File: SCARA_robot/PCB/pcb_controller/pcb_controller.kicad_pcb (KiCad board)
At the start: 2 copper layers, 24 parts, among them IC1 LD1117-3.3V-SOT223, J1 Barrel_Jack_Switch, J2 Conn_01x04_Pin_STEPPER_A, U1 LM7805CT, U2 ESP32-DEVKIT-V1

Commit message: schematic ready
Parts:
- added A2: Pololu_Breakout_DRV8825, Module:Pololu_Breakout-16_15.2x20.3mm, F.Cu at (224.3, 70.8)
- added A3: Pololu_Breakout_DRV8825, Module:Pololu_Breakout-16_15.2x20.3mm, F.Cu at (224.7, 46.5)
- added J10: interface, Connector_PinHeader_2.54mm:PinHeader_1x04_P2.54mm_Vertical, F.Cu at (126.6, 60.9)
- added J11: Conn_01x07_Socket, Connector_JST:JST_XH_S7B-XH-A-1_1x07_P2.50mm_Horizontal, F.Cu at (158.6, 139.5)
- added J12: Encoder_A, Connector_JST:JST_XH_B7B-XH-AM_1x07_P2.50mm_Vertical, F.Cu at (118.6, 28.9)
- added J13: Encoder_B, Connector_JST:JST_XH_B7B-XH-AM_1x07_P2.50mm_Vertical, F.Cu at (118.6, 36.7)
- added J14: Encoder_C, Connector_JST:JST_XH_B7B-XH-AM_1x07_P2.50mm_Vertical, F.Cu at (118.6, 44.5)
- added J15: Conn_01x04_Pin_STEPPER_B, Connector_JST:JST_XH_B4B-XH-AM_1x04_P2.50mm_Vertical, F.Cu at (115.3, 116.9)
- added J16: Conn_01x04_Pin_STEPPER_C, Connector_JST:JST_XH_B4B-XH-AM_1x04_P2.50mm_Vertical, F.Cu at (115.3, 124.7)
- added J3: interface, Connector_PinHeader_2.54mm:PinHeader_1x04_P2.54mm_Vertical, F.Cu at (157.8, 125.3)
- added J4: power, Connector_PinHeader_2.54mm:PinHeader_1x03_P2.54mm_Vertical, F.Cu at (117.4, 51.2)
- added J5: Conn_01x07_Socket, Connector_JST:JST_XH_S7B-XH-A-1_1x07_P2.50mm_Horizontal, F.Cu at (96.6, 30.4)
- added J6: power, Connector_PinHeader_2.54mm:PinHeader_1x03_P2.54mm_Vertical, F.Cu at (122.0, 51.2)
- added J7: interface, Connector_PinHeader_2.54mm:PinHeader_1x04_P2.54mm_Vertical, F.Cu at (122.0, 60.9)
- added J8: Conn_01x07_Socket, Connector_JST:JST_XH_S7B-XH-A-1_1x07_P2.50mm_Horizontal, F.Cu at (96.6, 44.0)
- added J9: power, Connector_PinHeader_2.54mm:PinHeader_1x03_P2.54mm_Vertical, F.Cu at (126.6, 51.2)
- added JP1: sel_encoderA, Jumper:SolderJumper-3_P1.3mm_Open_RoundedPad1.0x1.5mm, F.Cu at (131.7, 60.3)
- added JP2: sel_encoderB, Jumper:SolderJumper-3_P1.3mm_Open_RoundedPad1.0x1.5mm, F.Cu at (131.7, 64.2)
- added JP3: sel_encoderC, Jumper:SolderJumper-3_P1.3mm_Open_RoundedPad1.0x1.5mm, F.Cu at (131.7, 68.0)
- added JP4: SolderJumper_2_Open, Jumper:SolderJumper-2_P1.3mm_Open_RoundedPad1.0x1.5mm, F.Cu at (131.1, 53.8)
- added JP5: SolderJumper_2_Open, Jumper:SolderJumper-2_P1.3mm_Open_RoundedPad1.0x1.5mm, F.Cu at (124.8, 93.4)
- added JP6: SolderJumper_2_Open, Jumper:SolderJumper-2_P1.3mm_Open_RoundedPad1.0x1.5mm, F.Cu at (124.8, 97.0)
- added R10: 10K, PCM_Resistor_THT_AKL:R_Axial_DIN0204_L3.6mm_D1.6mm_P5.08mm_Horizontal, F.Cu at (130.3, 50.5)
- added SW1: Microstep mode, Button_Switch_THT:SW_DIP_SPSTx03_Slide_9.78x9.8mm_W7.62mm_P2.54mm, F.Cu at (106.2, 80.8)
- added SW2: Microstep mode, Button_Switch_THT:SW_DIP_SPSTx03_Slide_9.78x9.8mm_W7.62mm_P2.54mm, F.Cu at (90.9, 116.7)
- added SW3: Microstep mode, Button_Switch_THT:SW_DIP_SPSTx03_Slide_9.78x9.8mm_W7.62mm_P2.54mm, F.Cu at (102.3, 116.7)
- moved A1 154.6 mm to (224.2, 93.4)
- moved U2 129.3 mm to (172.7, 74.6)
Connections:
- A1 pad 13: unconnected-(A1-~{RST}-Pad13) -> /baseM_rst
- A1 pad 14: unconnected-(A1-~{SLP}-Pad14) -> Net-(A1-~{SLP})
- A1 pad 15: unconnected-(A1-STEP-Pad15) -> /baseM_step
- A1 pad 16: unconnected-(A1-DIR-Pad16) -> /baseM_dir
- A1 pad 2: unconnected-(A1-~{FLT}-Pad2) -> Net-(A1-~{FLT})
- R1 pad 2: unconnected-(R1-Pad2) -> /sda_master
- R2 pad 2: unconnected-(R2-Pad2) -> /scl_master
- R4 pad 2: unconnected-(R4-Pad2) -> /sda_enA
- R5 pad 2: unconnected-(R5-Pad2) -> /scl_enA
- R6 pad 2: unconnected-(R6-Pad2) -> /sda_enB
- R7 pad 2: unconnected-(R7-Pad2) -> /scl_enB
- R8 pad 2: unconnected-(R8-Pad2) -> /sda_enC
- R9 pad 2: unconnected-(R9-Pad2) -> /scl_enC
- U2 pad 11: unconnected-(U2-D21-Pad11) -> /sda_master
- U2 pad 14: unconnected-(U2-D22-Pad14) -> /scl_master

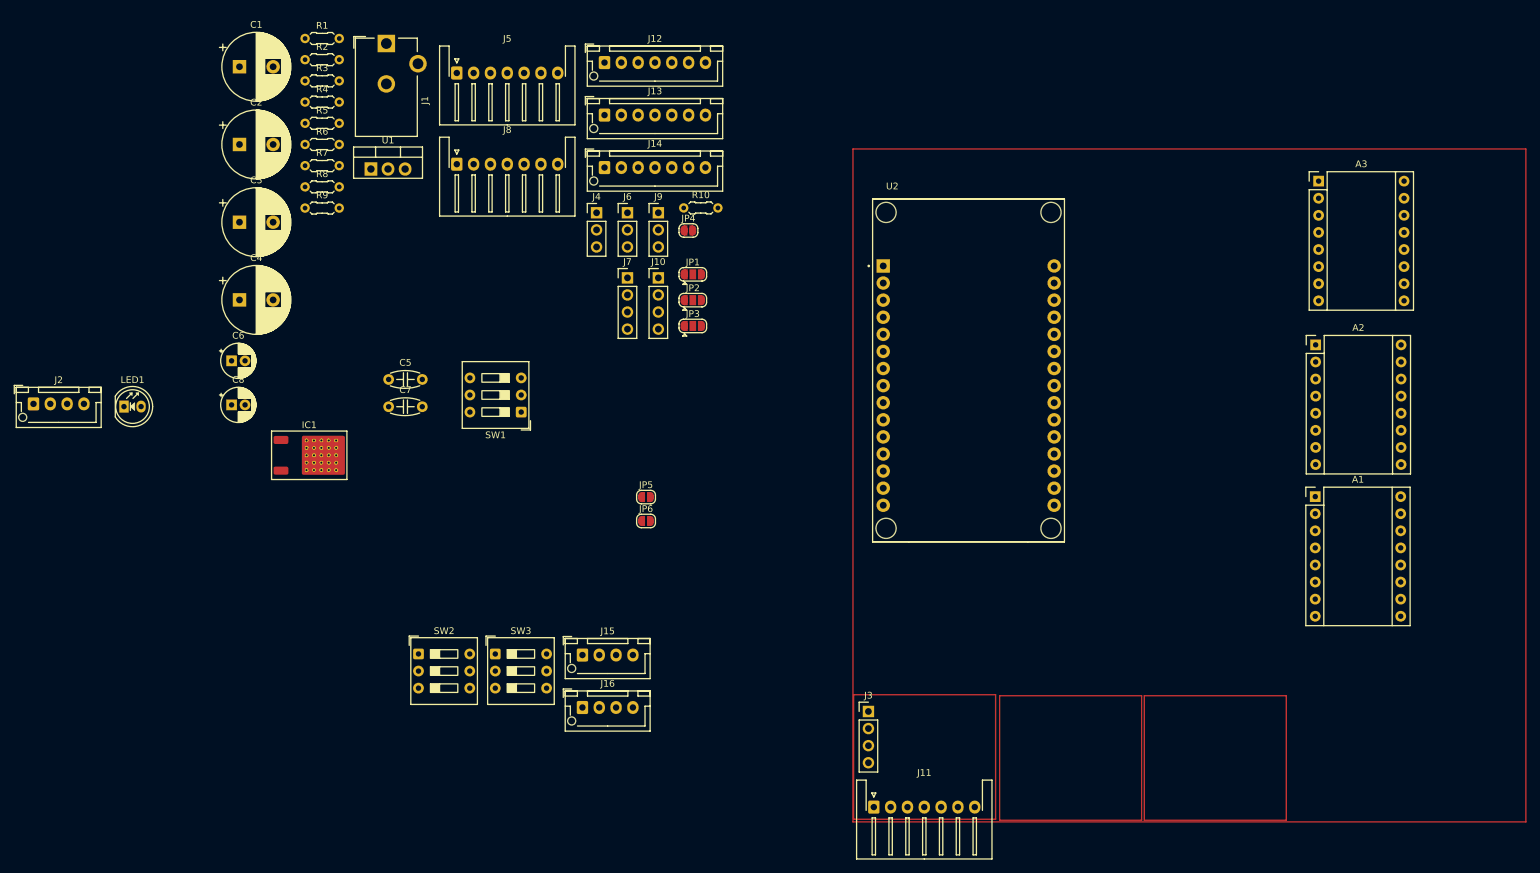
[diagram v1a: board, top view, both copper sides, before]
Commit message: schematic and footprints ready
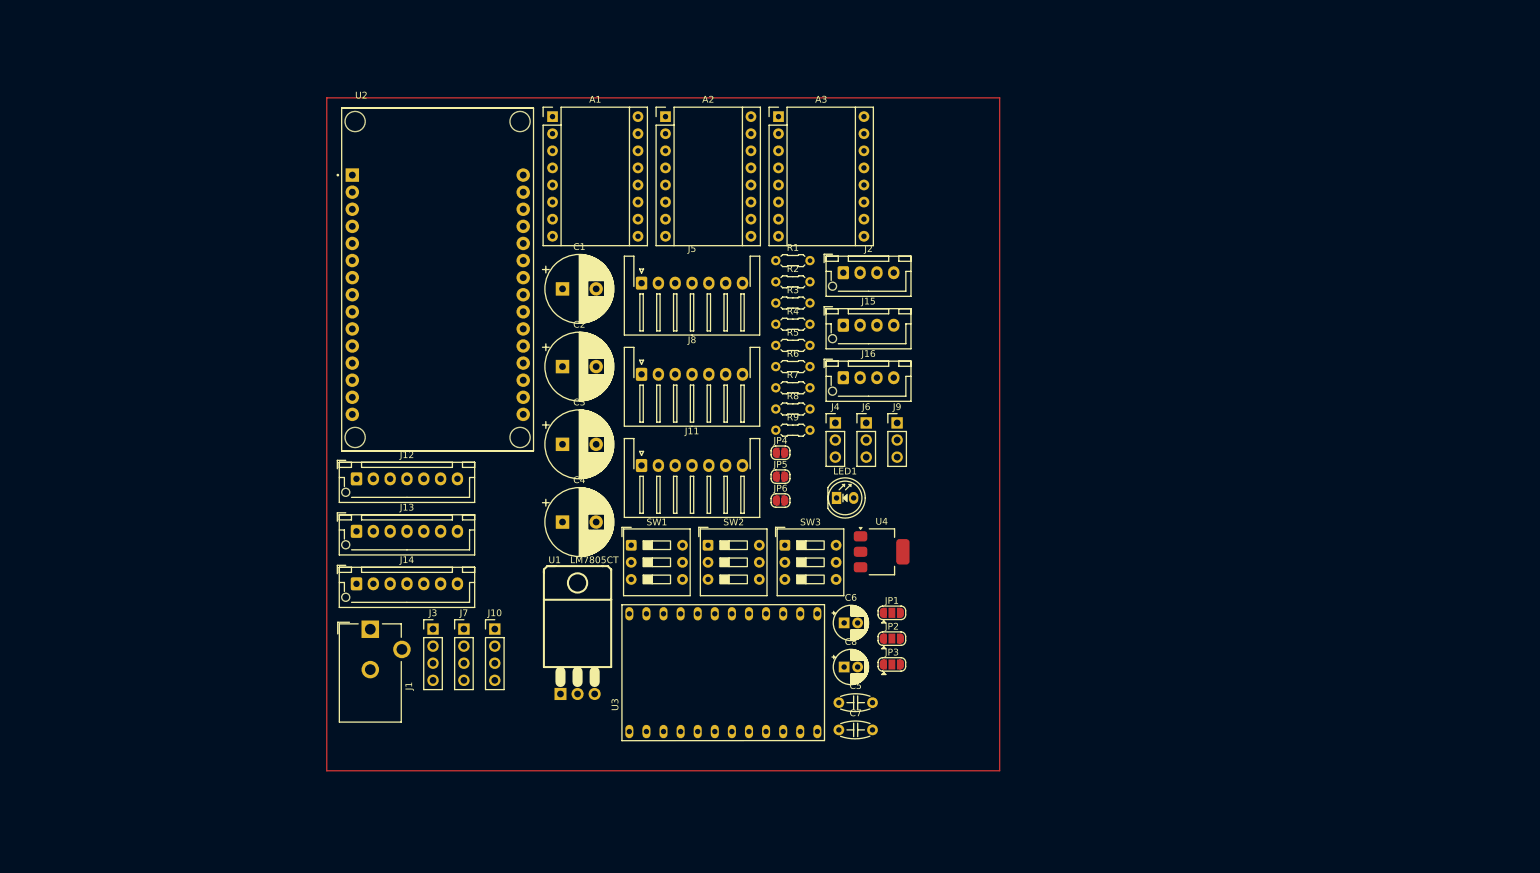
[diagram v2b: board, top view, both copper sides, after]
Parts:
- removed IC1: LD1117-3.3V-SOT223, PCM_Package_TO_SOT_SMD_AKL:TO-252-2_ThermalVias
- removed R10: 10K, PCM_Resistor_THT_AKL:R_Axial_DIN0204_L3.6mm_D1.6mm_P5.08mm_Horizontal
- added U3: PCA9548A, modules:TCA9548A, F.Cu at (136.2, 124.3)
- added U4: LD1117S33TR_SOT223, Package_TO_SOT_SMD:SOT-223-3_TabPin2, F.Cu at (159.8, 101.6)
- C1, C2, C3, C4: value 22uF 48v -> 47uF 48v
- U1: footprint PCM_Package_TO_SOT_THT_AKL:TO-220-3_Vertical -> PCM_4ms_Package_TO:TO-220-3_Horizontal
- moved A1 126.6 mm to (110.9, 36.9)
- moved J2 121.9 mm to (154.1, 60.1)
- moved LED1 106.8 mm to (153.1, 93.6)
- moved A2 102.4 mm to (127.6, 36.9)
- moved C8 99.0 mm to (154.2, 118.7)
- moved C6 99.0 mm to (154.2, 112.1)
- moved J1 87.1 mm to (83.8, 113.1)
- moved U1 83.8 mm to (114.6, 122.7)
- moved C5 82.4 mm to (153.4, 124.0)
- moved C7 82.4 mm to (153.4, 128.0)
- moved A3 80.8 mm to (144.4, 36.9)
- moved U2 80.0 mm to (93.8, 61.1)
- moved R1 77.4 mm to (144.0, 58.3)
- moved R2 77.4 mm to (144.0, 61.4)
- moved R3 77.4 mm to (144.0, 64.6)
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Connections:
- R1 pad 2: /sda_master -> /scl_master
- R2 pad 2: /scl_master -> /sda_master
- R4 pad 2: /sda_enA -> /scl_enA
- R5 pad 2: /scl_enA -> /sda_enA
- R6 pad 2: /sda_enB -> /scl_enB
- R7 pad 2: /scl_enB -> /sda_enB
- R8 pad 2: /sda_enC -> /scl_enC
- R9 pad 2: /scl_enC -> /sda_enC
- U2 pad 15: unconnected-(U2-D23-Pad15) -> /baseM_rst
- U2 pad 21: unconnected-(U2-D32-Pad21) -> /link2_dir
- U2 pad 22: unconnected-(U2-D33-Pad22) -> /link1_dir
- U2 pad 23: unconnected-(U2-D25-Pad23) -> /baseM_step
- U2 pad 24: unconnected-(U2-D26-Pad24) -> /link1_step
- U2 pad 25: unconnected-(U2-D27-Pad25) -> /link2_step
- U2 pad 28: unconnected-(U2-D13-Pad28) -> /baseM_dir
- U2 pad 4: unconnected-(U2-D2-Pad4) -> /rst_master
- U2 pad 6: unconnected-(U2-RX2-Pad6) -> /link2_rst
- U2 pad 7: unconnected-(U2-TX2-Pad7) -> /link1_rst

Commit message: pcb designed phase 1
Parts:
- removed J12: Encoder_A, Connector_JST:JST_XH_B7B-XH-AM_1x07_P2.50mm_Vertical
- removed J13: Encoder_B, Connector_JST:JST_XH_B7B-XH-AM_1x07_P2.50mm_Vertical
- removed J14: Encoder_C, Connector_JST:JST_XH_B7B-XH-AM_1x07_P2.50mm_Vertical
- removed R1, R2: 4K7, PCM_Resistor_THT_AKL:R_Axial_DIN0204_L3.6mm_D1.6mm_P5.08mm_Horizontal
- removed SW1, SW2, SW3: Microstep mode, Button_Switch_THT:SW_DIP_SPSTx03_Slide_9.78x9.8mm_W7.62mm_P2.54mm
- added D2: SS36, Diode_SMD:D_2114_3652Metric_Pad1.85x3.75mm_HandSolder, B.Cu at (138.6, 38.1)
- added H1: MountingHole, MountingHole:MountingHole_3.2mm_M3_ISO14580, F.Cu at (80.5, 37.3)
- added H2: MountingHole, MountingHole:MountingHole_3.2mm_M3_ISO14580, F.Cu at (174.1, 37.3)
- added H3: MountingHole, MountingHole:MountingHole_3.2mm_M3_ISO14580, F.Cu at (174.1, 121.8)
- added H4: MountingHole, MountingHole:MountingHole_3.2mm_M3_ISO14580, F.Cu at (80.5, 102.9)
- added J17: Conn_01x02_Pin, Connector_PinSocket_2.54mm:PinSocket_1x02_P2.54mm_Vertical, F.Cu at (86.0, 40.8)
- added J18: Conn_01x04_Pin_STEPPER_C, Connector_JST:JST_XH_B4B-XH-AM_1x04_P2.50mm_Vertical, F.Cu at (115.5, 96.9)
- added J19: Conn_01x04_Pin_STEPPER_C, Connector_JST:JST_XH_B4B-XH-AM_1x04_P2.50mm_Vertical, F.Cu at (101.8, 96.9)
- added J20: Conn_01x04_Pin_STEPPER_C, Connector_JST:JST_XH_B4B-XH-AM_1x04_P2.50mm_Vertical, F.Cu at (88.2, 96.9)
- added JP10: Jumper_2_Open, PCM_Jumper_AKL:Jumper_P2.54mm_D0.7mm, F.Cu at (146.1, 73.7)
- added JP11: Jumper_2_Open, PCM_Jumper_AKL:Jumper_P2.54mm_D0.7mm, F.Cu at (146.1, 76.8)
- added JP12: Jumper_2_Open, PCM_Jumper_AKL:Jumper_P2.54mm_D0.7mm, F.Cu at (146.1, 80.0)
- added JP13: Jumper_2_Open, PCM_Jumper_AKL:Jumper_P2.54mm_D0.7mm, F.Cu at (146.0, 99.3)
- added JP14: Jumper_2_Open, PCM_Jumper_AKL:Jumper_P2.54mm_D0.7mm, F.Cu at (146.0, 102.5)
- added JP15: Jumper_2_Open, PCM_Jumper_AKL:Jumper_P2.54mm_D0.7mm, F.Cu at (146.0, 105.6)
- added JP7: Jumper_2_Open, PCM_Jumper_AKL:Jumper_P2.54mm_D0.7mm, F.Cu at (146.2, 46.7)
- added JP8: Jumper_2_Open, PCM_Jumper_AKL:Jumper_P2.54mm_D0.7mm, F.Cu at (146.2, 49.8)
- added JP9: Jumper_2_Open, PCM_Jumper_AKL:Jumper_P2.54mm_D0.7mm, F.Cu at (146.2, 53.0)
- JP4, JP5, JP6, R4, R5, R6, R7, R8, R9, U1, U4: moved to B.Cu
- moved C5 86.1 mm to (132.0, 40.6), turned to 90 degrees
- moved J1 84.5 mm to (138.7, 48.8), turned to 180 degrees
- moved A3 82.8 mm to (164.0, 117.3), turned to 180 degrees
- moved C6 80.4 mm to (126.5, 36.6), turned to -90 degrees
- moved LED1 80.4 mm to (94.1, 38.9), turned to 90 degrees
- moved J5 77.6 mm to (80.5, 125.8)
- moved J4 74.3 mm to (84.1, 110.4)
- moved C4 74.3 mm to (156.5, 37.4), turned to -90 degrees
- moved U1 71.8 mm to (84.4, 57.5), turned to 90 degrees
- moved JP1 71.7 mm to (90.0, 117.9)
- moved C7 69.7 mm to (109.7, 73.8), turned to -90 degrees
- moved A2 65.9 mm to (164.2, 91.7), turned to 180 degrees
- moved R9 64.6 mm to (79.4, 83.9), turned to -90 degrees
- moved U3 63.6 mm to (92.8, 77.9), turned to 180 degrees
- moved R8 62.5 mm to (81.7, 83.9), turned to -90 degrees
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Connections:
- J1 pad 1: +12V -> Net-(D2-A)
- J15 pad 3: Net-(A2-A2) -> Net-(A2-A1)
- J15 pad 4: Net-(A2-A1) -> Net-(A2-A2)
- J16 pad 3: Net-(A3-A2) -> Net-(A3-A1)
- J16 pad 4: Net-(A3-A1) -> Net-(A3-A2)
- J2 pad 3: Net-(A1-A2) -> Net-(A1-A1)
- J2 pad 4: Net-(A1-A1) -> Net-(A1-A2)
- U2 pad 30: +5V -> Net-(J17-Pin_2)
- U3 pad 15: /scl_enB -> unconnected-(U3-sc6-Pad15)
- U3 pad 16: /sda_enB -> unconnected-(U3-sd6-Pad16)
- U3 pad 17: /scl_enC -> unconnected-(U3-sc5-Pad17)
- U3 pad 18: /sda_enC -> unconnected-(U3-sd5-Pad18)
- U3 pad 19: unconnected-(U3-sc4-Pad19) -> /scl_enB
- U3 pad 20: unconnected-(U3-sd4-Pad20) -> /sda_enB
- U3 pad 23: unconnected-(U3-sc2-Pad23) -> /scl_enC
- U3 pad 24: unconnected-(U3-sd2-Pad24) -> /sda_enC
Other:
- board outline added: 100 x 100 mm

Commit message: pcb designed phase 2
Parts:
- U4: moved to F.Cu
- moved D2 58.1 mm to (81.1, 46.5), turned to -90 degrees
- moved J17 56.5 mm to (142.5, 39.7), turned to 0 degrees
- moved C6 51.3 mm to (79.7, 57.7), turned to 0 degrees
- moved C5 50.0 mm to (83.6, 53.1), turned to 180 degrees
- moved J1 47.0 mm to (91.8, 46.4), turned to -90 degrees
- moved U1 46.1 mm to (129.1, 46.2), turned to 0 degrees
- moved C8 36.9 mm to (98.3, 47.2), turned to 90 degrees
- moved U4 29.7 mm to (105.7, 50.3), turned to 180 degrees
- moved C7 29.4 mm to (103.8, 45.0), turned to 0 degrees
- moved U2 23.0 mm to (126.0, 61.4), turned to 0 degrees
- moved R3 19.0 mm to (84.9, 38.7), turned to 0 degrees
- moved R4 10.8 mm to (106.6, 79.0), turned to -90 degrees
- moved R5 8.86 mm to (104.2, 79.0), turned to -90 degrees
- moved J3 7.38 mm to (96.3, 116.3), turned to 180 degrees
- moved JP1 7.31 mm to (87.9, 110.9), turned to 90 degrees
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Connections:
- JP8 pad 1: unconnected-(JP8-A-Pad1) -> +3.3V
- U2 pad 15: /baseM_rst -> /link2_rst
- U2 pad 24: /link1_step -> /link2_step
- U2 pad 25: /link2_step -> /link1_step
- U2 pad 6: /link2_rst -> /baseM_rst
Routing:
- net +12V: track 0.00 -> 269.8 mm
- net +3.3V: track 0.00 -> 263.5 mm, vias 0 -> 2
- net /link1_rst: track 0.00 -> 68.6 mm, vias 0 -> 1
- net /link2_rst: track 0.00 -> 67.2 mm, vias 0 -> 1
- net /link2_step: track 0.00 -> 62.3 mm, vias 0 -> 1
- net /baseM_rst: track 0.00 -> 60.9 mm
- net +5V: track 0.00 -> 59.7 mm
- net /link2_dir: track 0.00 -> 57.9 mm
- net /link1_step: track 0.00 -> 42.1 mm, vias 0 -> 2
- net /link1_dir: track 0.00 -> 36.9 mm
- net /rst_master: track 0.00 -> 30.4 mm
- net /baseM_dir: track 0.00 -> 22.9 mm, vias 0 -> 2
- net /scl_master: track 0.00 -> 22.0 mm
- net /baseM_step: track 0.00 -> 13.5 mm
- net /sda_master: track 0.00 -> 13.4 mm
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- added copper zone on B.Cu, net GNDA
